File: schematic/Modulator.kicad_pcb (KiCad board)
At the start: 2 copper layers, 160 x 100 mm, 27 parts, among them J1 VIDEO IN, J2 VIDEO OUT, J3 MA18-2, J4 MA05-2, U1 74590N, U2 IDT72125, U3 74590N, U4 7404N, U5 LM1881N, U6 7408N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

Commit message: First draft of PCB routing
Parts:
- removed U$1: , Modulator:LOGO
- removed U$2: , Modulator:JOLLYROGER
- added D1: D_Zener, Diode_THT:D_DO-41_SOD81_P7.62mm_Horizontal, F.Cu at (207.0, 61.0)
- added D2: D, Diode_THT:D_DO-41_SOD81_P7.62mm_Horizontal, F.Cu at (201.2, 61.0)
- added J5: PJ-002B, PJ-002B:CUI_PJ-002B, F.Cu at (218.4, 67.3)
- added R1: 5.1kR, Resistor_THT:R_Axial_DIN0207_L6.3mm_D2.5mm_P10.16mm_Horizontal, F.Cu at (182.9, 72.4)
- added R3: 5.1kR, Resistor_THT:R_Axial_DIN0207_L6.3mm_D2.5mm_P10.16mm_Horizontal, F.Cu at (182.9, 67.3)
- added U10: TXS0108EPW, Package_SO:TSSOP-20_4.4x6.5mm_P0.65mm, F.Cu at (83.8, 113.5)
- added U11: TXS0108EPW, Package_SO:TSSOP-20_4.4x6.5mm_P0.65mm, F.Cu at (83.8, 80.0)
- added U12: TXS0108EPW, Package_SO:TSSOP-20_4.4x6.5mm_P0.65mm, F.Cu at (83.8, 96.8)
- added U9: RASPBERRY_PI_ZERO_2_W, RASPBERRY_PI_ZERO_2_W:MODULE_RASPBERRY_PI_ZERO_2_W, F.Cu at (78.8, 99.1)
- J3: value MA18-2 -> 10164359-00011LF; footprint Modulator:MA18-2 -> 10164359_00011LF:AMPHENOL_10164359-00011LF; moved to F.Cu
- J4: footprint Modulator:MA05-2 -> AD9834:AD9834
- U2: footprint Modulator:SO28L -> Package_DIP:DIP-28_W7.62mm_LongPads
- moved J3 118.3 mm to (187.5, 58.4), turned to 180 degrees
- moved X2 44.2 mm to (209.6, 88.9)
- moved C3 43.4 mm to (209.6, 76.2)
- moved U2 29.1 mm to (110.6, 124.0), turned to 180 degrees
- moved J4 26.4 mm to (198.1, 125.7), turned to 90 degrees
- moved C13 19.8 mm to (189.2, 78.7), turned to 0 degrees
- moved U8 18.7 mm to (189.2, 89.9)
- moved C14 9.30 mm to (106.4, 87.1), turned to 0 degrees
- moved C5 1.08 mm to (110.4, 81.5)
- moved C12 0.18 mm to (150.9, 63.6)
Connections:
- net Net-(U4D-O) renamed /RST
- net Net-(U8A-O) renamed /FS
- J4 pad 1: /DDSCS -> /FSY
- J4 pad 5: /MOSI -> /SDA
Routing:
- net /SDA: track 0.00 -> 201.3 mm, vias 0 -> 2
- net /DDSCS: track 190.1 -> 0.00 mm, vias 2 -> 0
- net /MOSI: track 186.2 -> 0.00 mm
- net /FSY: track 0.00 -> 185.6 mm, vias 0 -> 2
- net +3V3: track 0.00 -> 74.8 mm
- net +5V: track 575.1 -> 630.3 mm, vias 5 -> 3
- net /RST: track 155.2 -> 100.0 mm
- net /D0: track 14.9 -> 68.7 mm, vias 0 -> 1
- net /D1: track 18.0 -> 64.0 mm, vias 0 -> 1
- net /D2: track 14.9 -> 58.1 mm, vias 0 -> 2
- net /D4: track 14.9 -> 56.4 mm, vias 0 -> 2
- net /D3: track 18.0 -> 57.3 mm, vias 0 -> 2
- net /D6: track 14.9 -> 52.6 mm, vias 0 -> 2
- net /D5: track 18.0 -> 54.6 mm, vias 0 -> 2
- net Net-(U1A-CLK): track 132.0 -> 168.3 mm
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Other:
- board size 160 x 100 mm -> 170 x 100 mm
- board text added: "Original Design: Techknight Updated by Jesse Cardone"
- board text added: "Pi Zero 2W"
- board text added: "The Weather STAR Revamped 7.38Mhz FSK Encoder"
- board text removed: "Raspberry Pi Zero 2W"
- board text removed: "Techknight"
- board text removed: "The Weather STAR Reborn 7.38Mhz FSK Encoder"

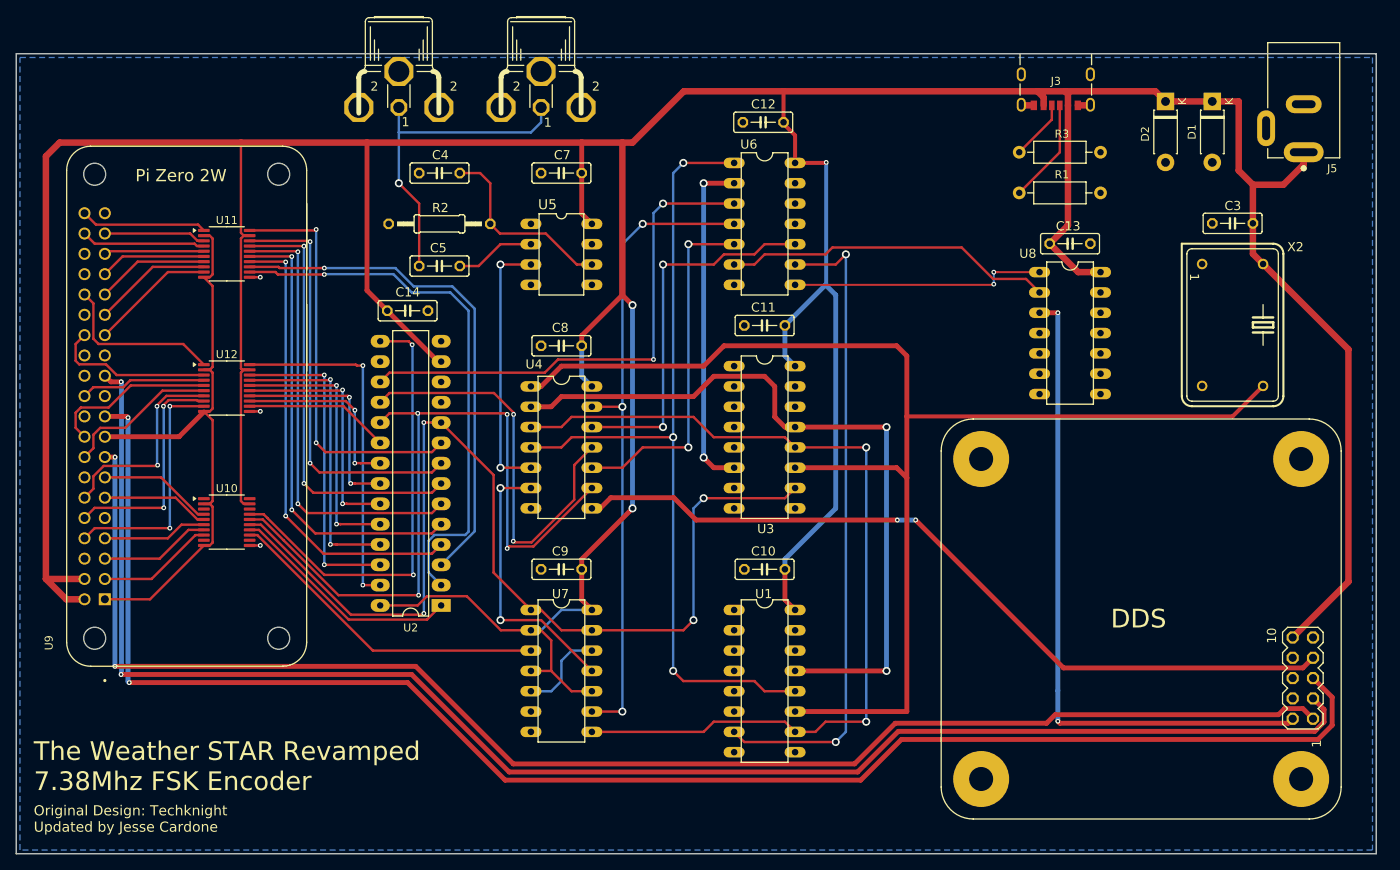
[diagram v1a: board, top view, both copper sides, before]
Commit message: Make room for SMA connectors on DDS board
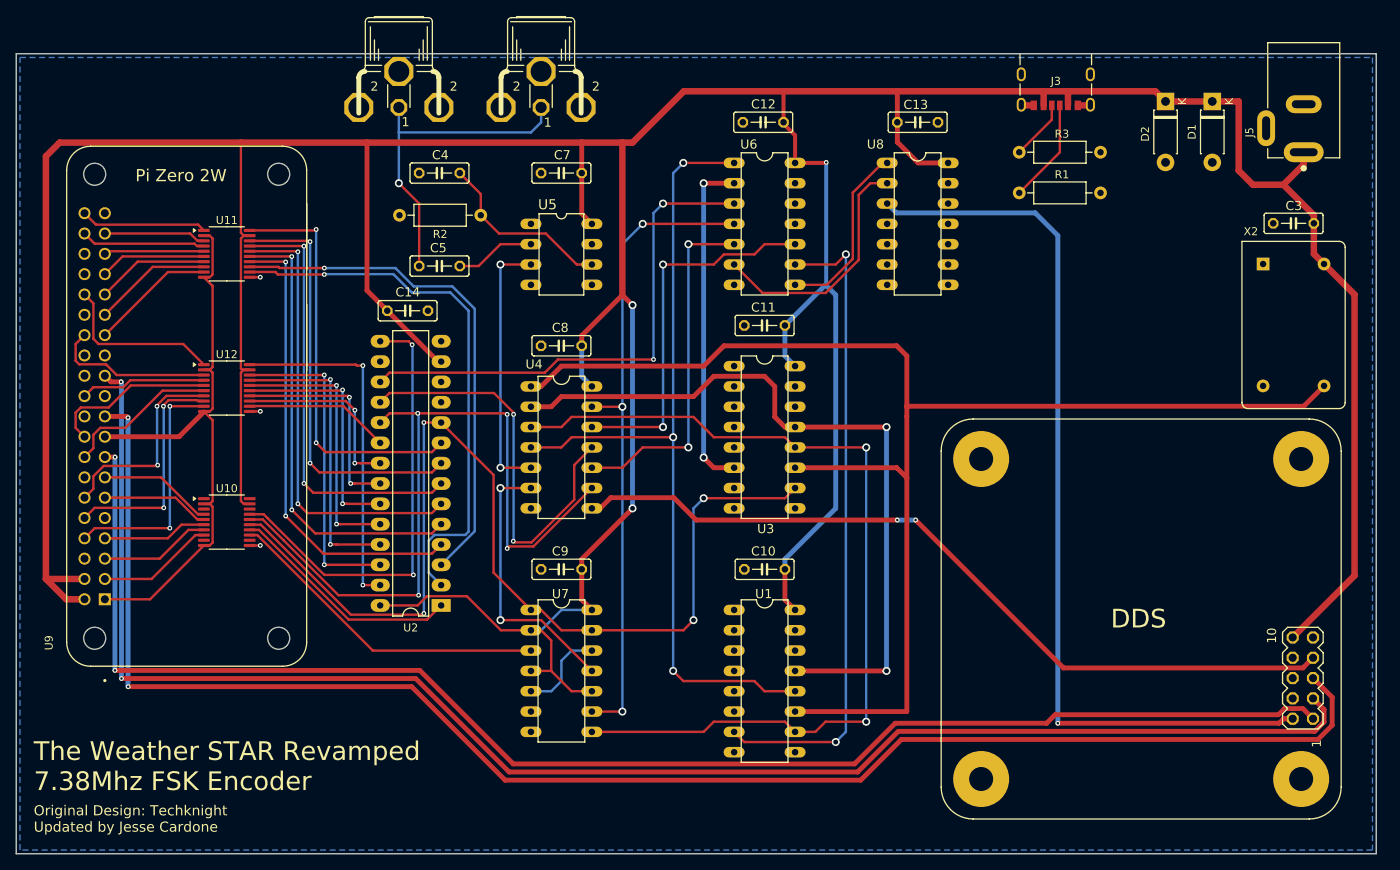
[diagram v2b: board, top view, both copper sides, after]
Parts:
- R2: footprint Modulator:0207_12 -> Resistor_THT:R_Axial_DIN0207_L6.3mm_D2.5mm_P10.16mm_Horizontal
- X2: footprint Modulator:DIL14S -> Oscillator:Oscillator_DIP-14
- moved C13 24.4 mm to (170.2, 63.6)
- moved U8 23.4 mm to (170.2, 76.3)
- moved X2 8.52 mm to (213.4, 81.3)
- moved C3 7.62 mm to (217.2, 76.2)
- moved R2 5.27 mm to (115.6, 75.2)
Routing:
- net /FS: track 83.0 -> 113.5 mm, vias 2 -> 1
- net +5V: track 630.3 -> 616.7 mm
- net Net-(U6B-O): track 41.4 -> 31.0 mm
- net Net-(U6C-O): track 32.1 -> 22.7 mm, vias 2 -> 0
- net Net-(U1A-CLK): track 168.3 -> 175.7 mm
- net Net-(U5A-RSET): track 24.2 -> 22.8 mm

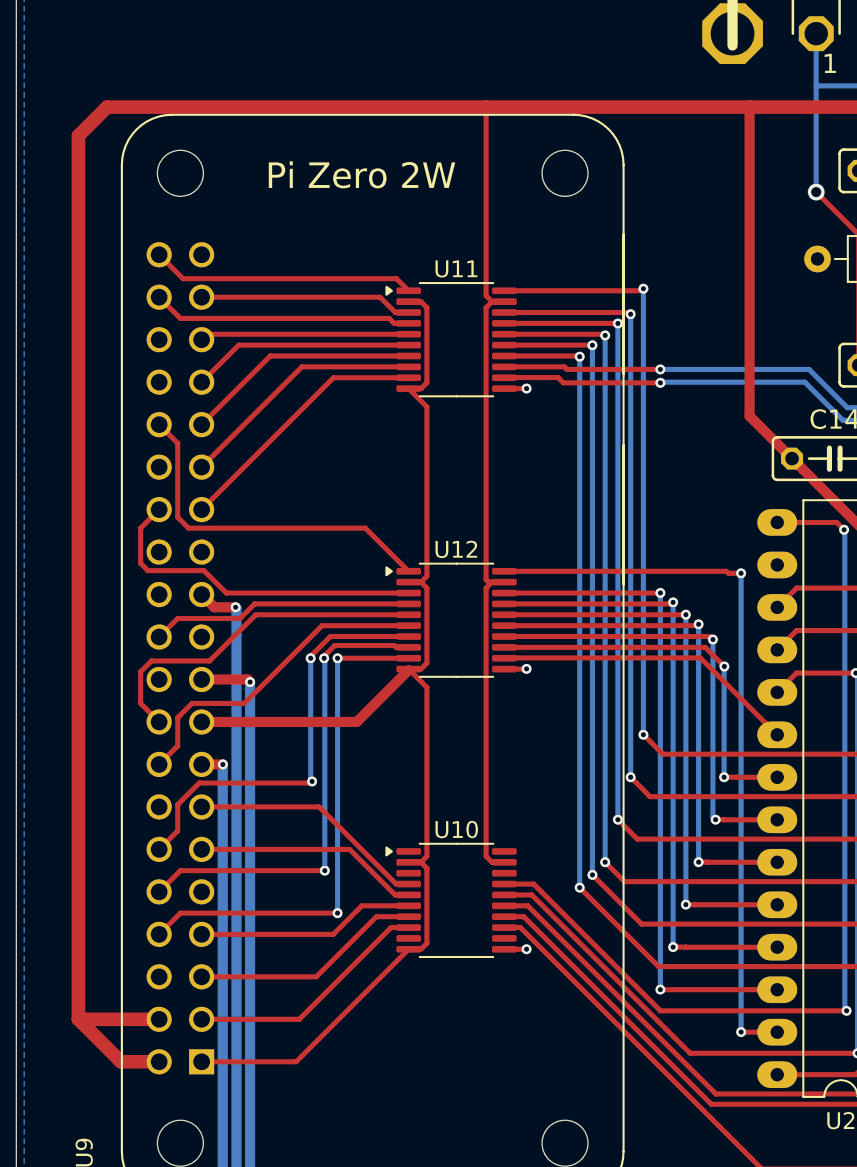
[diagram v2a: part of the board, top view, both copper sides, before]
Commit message: Add decoupling capacitors to level shifters
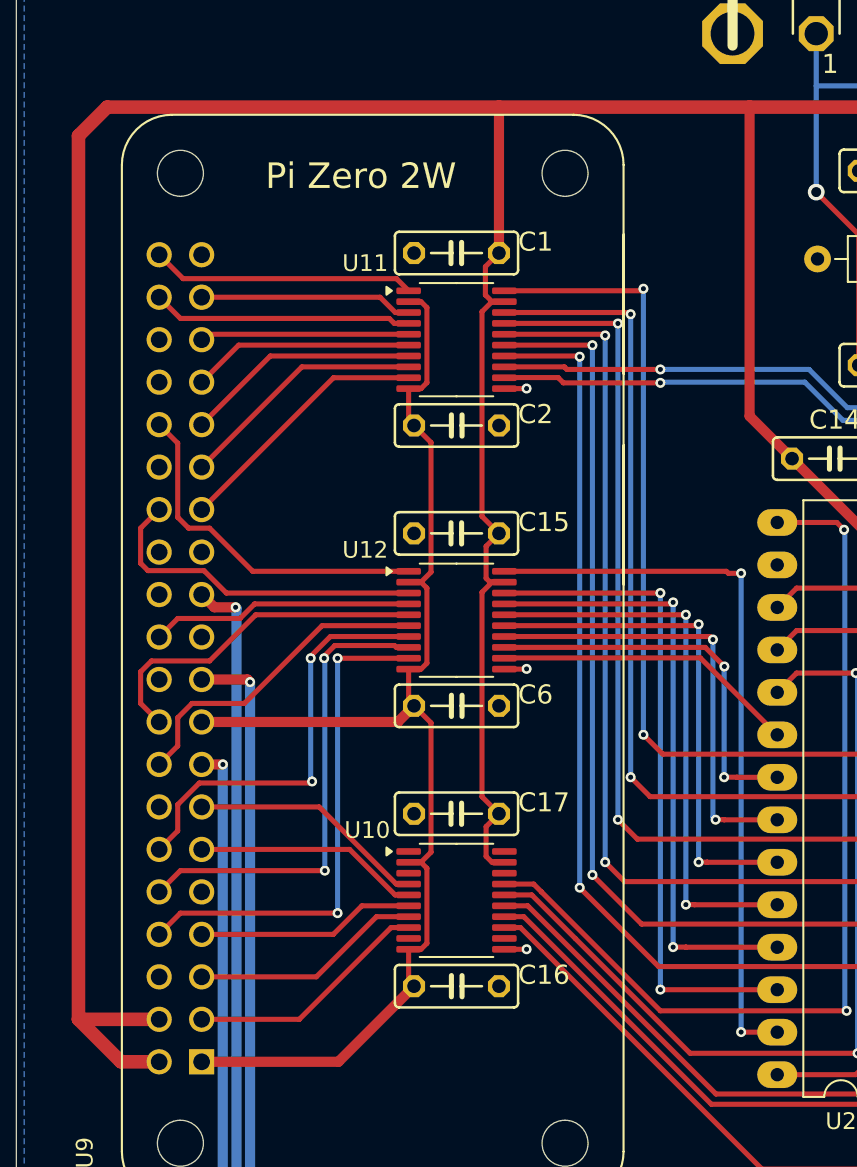
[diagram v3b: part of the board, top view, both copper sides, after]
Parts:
- added C1: 100nF, Modulator:C050-025X075, F.Cu at (83.8, 74.8)
- added C15: 100nF, Modulator:C050-025X075, F.Cu at (83.8, 91.6)
- added C16: 100nF, Modulator:C050-025X075, F.Cu at (83.8, 118.7)
- added C17: 100nF, Modulator:C050-025X075, F.Cu at (83.8, 108.4)
- added C2: 100nF, Modulator:C050-025X075, F.Cu at (83.8, 85.1)
- added C6: 100nF, Modulator:C050-025X075, F.Cu at (83.8, 101.9)
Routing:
- net +5V: track 616.7 -> 618.6 mm
- net +3V3: track 74.8 -> 76.4 mm

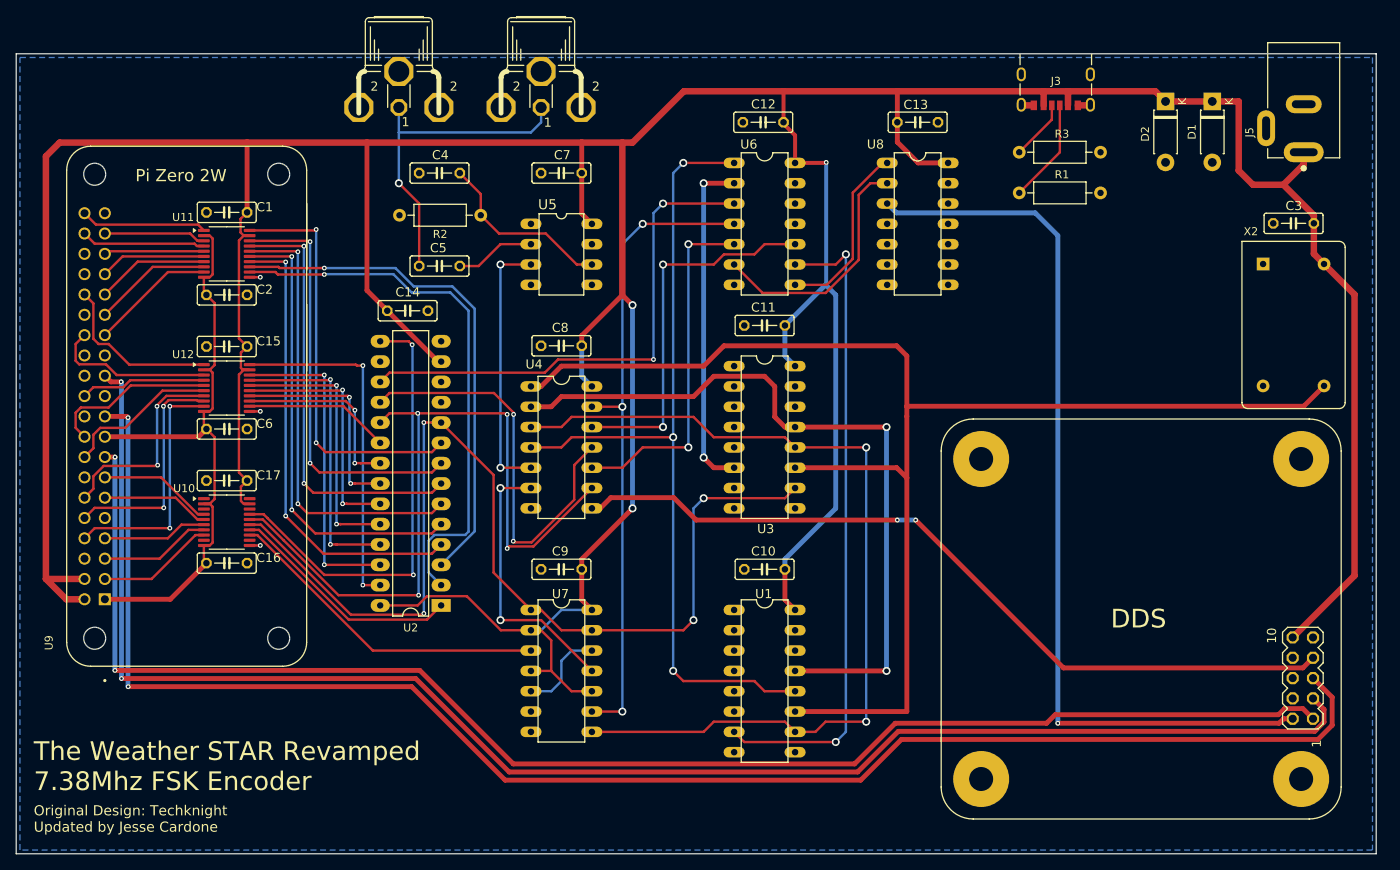
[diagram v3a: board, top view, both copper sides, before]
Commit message: Change some decoupling capacitors, and usb-c resistors to SMT
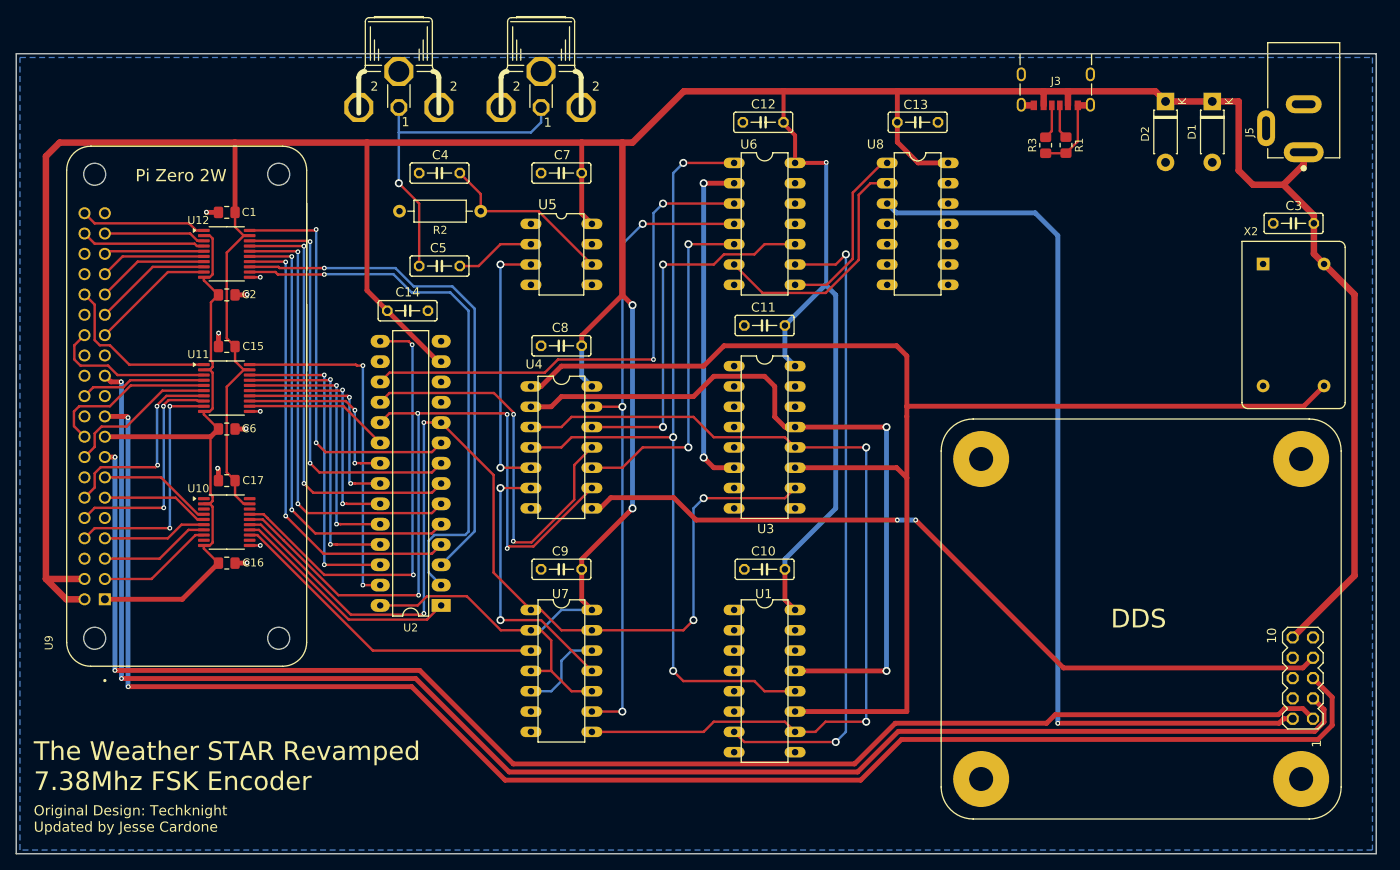
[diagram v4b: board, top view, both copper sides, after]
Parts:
- C1, C15, C16, C17, C2, C6: footprint Modulator:C050-025X075 -> Capacitor_SMD:C_0805_2012Metric_Pad1.18x1.45mm_HandSolder
- R1, R3: footprint Resistor_THT:R_Axial_DIN0207_L6.3mm_D2.5mm_P10.16mm_Horizontal -> Resistor_SMD:R_0805_2012Metric_Pad1.20x1.40mm_HandSolder
- moved R1 8.35 mm to (188.7, 66.4), turned to -90 degrees
- moved R3 3.42 mm to (186.2, 66.4), turned to -90 degrees
- moved R2 0.51 mm to (115.6, 74.7)
- renumbered U12 to U11, U11 to U12
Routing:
- net GND: track 7.20 -> 25.6 mm, vias 3 -> 9
- net Net-(J3-CC1): track 13.0 -> 4.29 mm
- net +3V3: track 76.4 -> 81.2 mm
- net Net-(J3-CC2): track 7.55 -> 4.31 mm

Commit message: Update capacitor footprints
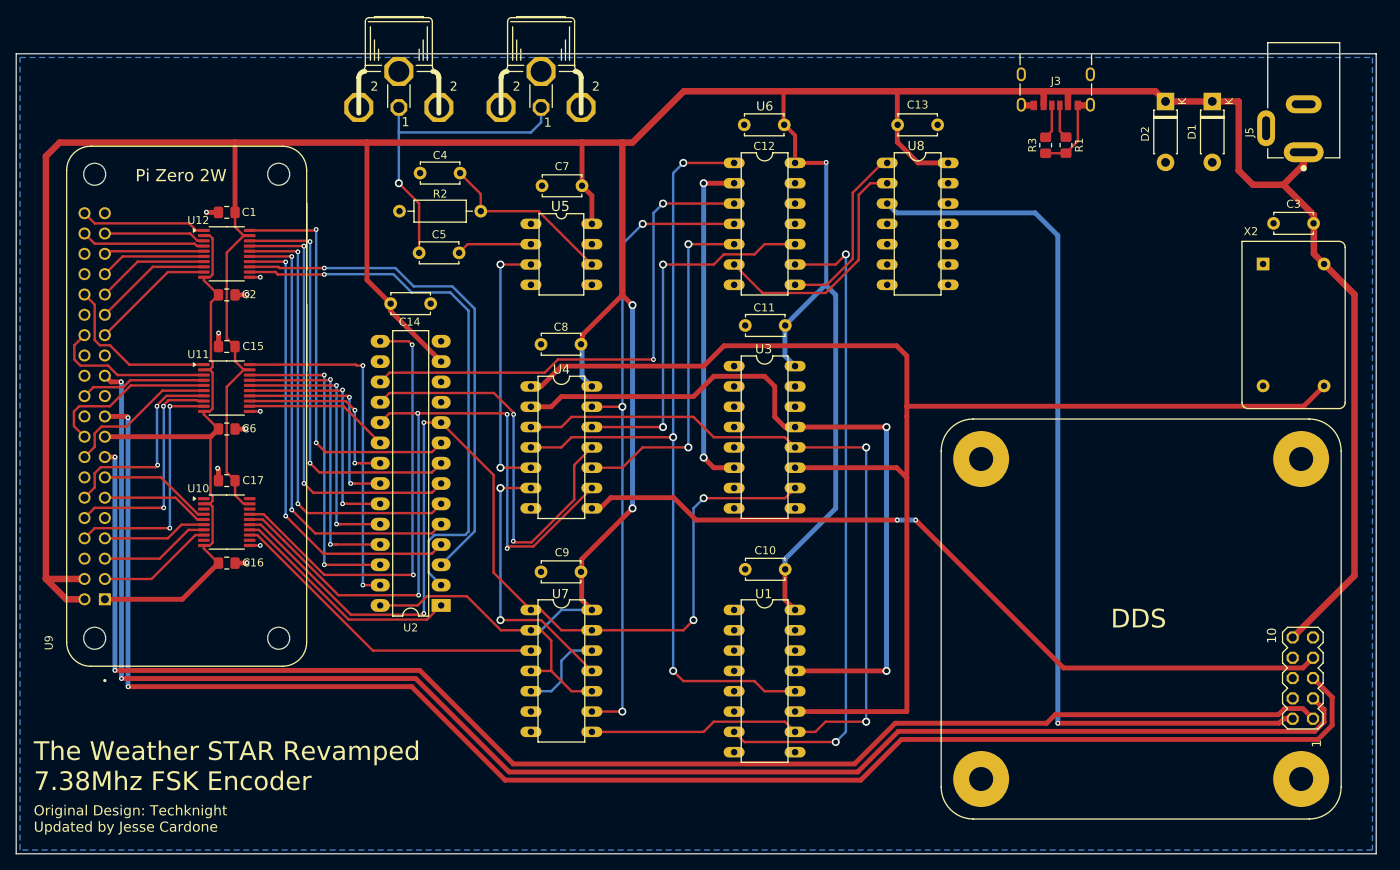
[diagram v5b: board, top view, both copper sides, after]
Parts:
- C10, C11, C12, C13, C14, C3, C4, C5, C7, C8, C9: footprint Modulator:C050-025X075 -> Capacitor_THT:C_Disc_D4.7mm_W2.5mm_P5.00mm
- moved C7 3.03 mm to (128.2, 71.5)
- moved C5 2.96 mm to (112.9, 79.9)
- moved C12 2.65 mm to (153.5, 63.9)
- moved C10 2.58 mm to (153.6, 119.4)
- moved C11 2.58 mm to (153.6, 89.0)
- moved C4 2.58 mm to (113.0, 69.9)
- moved C13 2.52 mm to (167.7, 63.9)
- moved C3 2.50 mm to (219.7, 76.2)
- moved C9 2.47 mm to (128.1, 119.8)
- moved C8 2.46 mm to (128.1, 91.3)
- moved C14 2.30 mm to (104.3, 86.2)
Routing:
- net Net-(C5-Pad2): track 41.0 -> 39.4 mm
- net Net-(U5A-VIDEO): track 10.0 -> 9.43 mm
